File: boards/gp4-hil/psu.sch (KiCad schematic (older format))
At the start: 76 parts, among them K1 CONN_3_PWROUT, Q11 SSM6N58NU, Q12 DMP2069UFY4, U1 MIC2288-DFN, U20 SIP32408, U21 SIP32408, U22 SIP32408, U23 SIP32408, U24 SIP32408, U3 LTC3374-QFN, U4 SIP32408

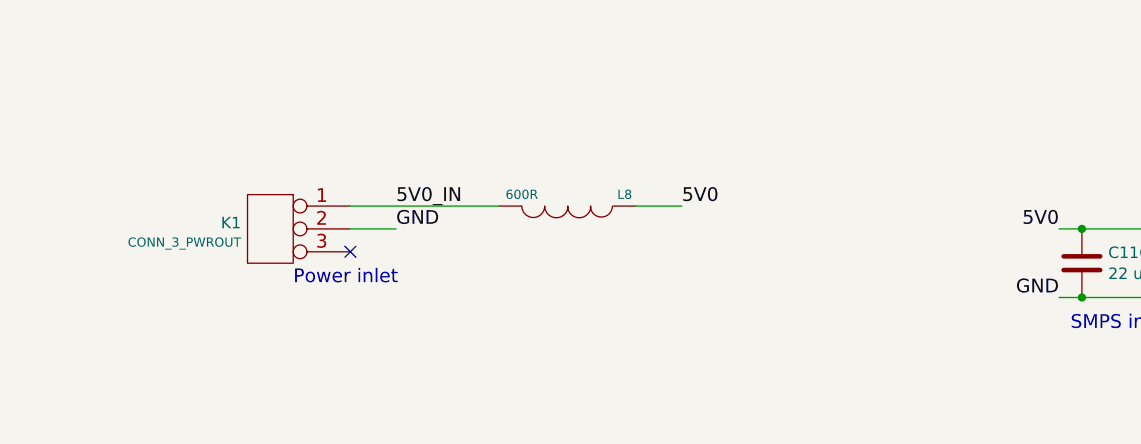
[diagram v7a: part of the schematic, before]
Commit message: Added reverse polarity protection and fusing to input
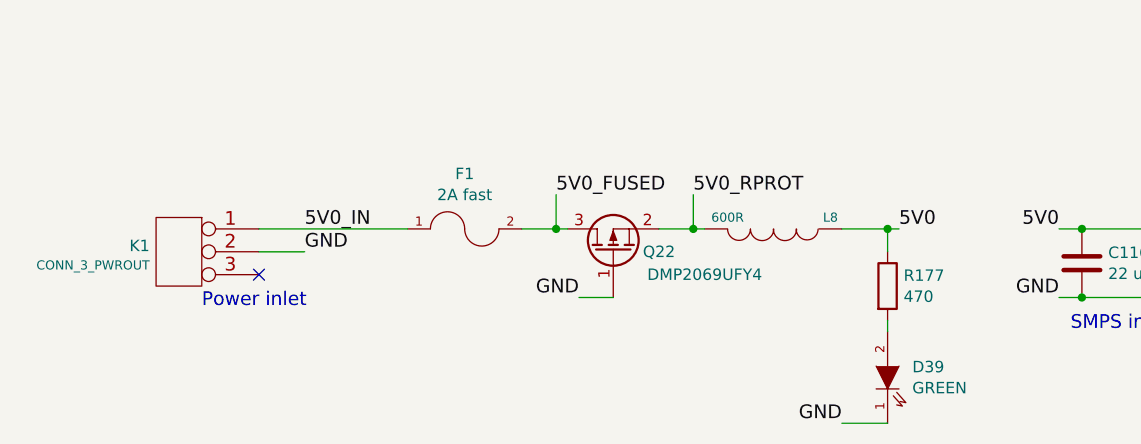
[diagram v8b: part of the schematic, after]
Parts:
- added D39: GREEN, symbol LED
- added F1: 2A fast, symbol FUSE
- added Q22: DMP2069UFY4, symbol Q_PMOS_GSD
- added R177: 470, symbol R
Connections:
- net 5V0: now also R177.1
- net 5V0_IN: now also F1.1; no longer L8.2
- net GND: now also D39.1 (K), Q22.1 (G)
- new net: D39.2 (A), R177.2
- new net 5V0_FUSED: F1.2, Q22.3 (D)
- new net 5V0_RPROT: L8.2, Q22.2 (S)
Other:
- moved on the sheet: K1, L8
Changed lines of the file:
@@
 	1    0    0    -1
 $EndComp
-Text Label 2250 15000 0    60   ~ 0
+Text Label 1850 15100 0    60   ~ 0
 5V0_IN
-Text Label 2250 15100 0    60   ~ 0
-GND
-NoConn ~ 2050 15200
-Text Notes 1800 15350 0    60   ~ 0
+Text Label 1850 15200 0    60   ~ 0
+GND
+NoConn ~ 1650 15300
+Text Notes 1400 15450 0    60   ~ 0
 Power inlet
 $Comp
 L CONN_3_PWROUT K1
 U 1 1 573DEBE1
-P 1700 15100
-F 0 "K1" H 1828 15126 50  0000 L CNN
-F 1 "CONN_3_PWROUT" H 1828 15041 40  0000 L CNN
-F 2 "" H 1700 15100 60  0000 C CNN
-F 3 "" H 1700 15100 60  0000 C CNN
-	1    1700 15100
+P 1300 15200
+F 0 "K1" H 1428 15226 50  0000 L CNN
+F 1 "CONN_3_PWROUT" H 1428 15141 40  0000 L CNN
+F 2 "" H 1300 15200 60  0000 C CNN
+F 3 "" H 1300 15200 60  0000 C CNN
+	1    1300 15200
 	-1   0    0    -1
 $EndComp
@@
 L INDUCTOR_PWROUT L8
 U 1 1 57402179
-P 3000 15000
-F 0 "L8" V 2950 15250 40  0000 C CNN
-F 1 "600R" V 2950 14800 40  0000 C CNN
-F 2 "" H 3000 15000 60  0000 C CNN
-F 3 "" H 3000 15000 60  0000 C CNN
-	1    3000 15000
-	0    1    1    0
-$EndComp
-Text Label 3500 15000 0    60   ~ 0
+P 3900 15100
+F 0 "L8" V 3850 15350 40  0000 C CNN
+F 1 "600R" V 3850 14900 40  0000 C CNN
+F 2 "" H 3900 15100 60  0000 C CNN
+F 3 "" H 3900 15100 60  0000 C CNN
+	1    3900 15100
+	0    1    1    0
+$EndComp
+Text Label 4450 15100 0    60   ~ 0
 5V0
 Text HLabel 4550 8550 2    60   Output ~ 0
@@
 Text Label 21050 3750 2    60   ~ 0
 PSU_VTEMP
-Wire Wire Line
-	2050 15000 2700 15000
-Wire Wire Line
-	2250 15100 2050 15100
+$Comp
+L FUSE F1
+U 1 1 5764BE84
+P 2550 15100
+F 0 "F1" H 2550 15341 50  0000 C CNN
+F 1 "2A fast" H 2550 15249 50  0000 C CNN
+F 2 "" H 2550 15100 60  0000 C CNN
+F 3 "" H 2550 15100 60  0000 C CNN
+	1    2550 15100
+	1    0    0    -1
+$EndComp
+$Comp
+L Q_PMOS_GSD Q22
+U 1 1 5764DB2D
+P 3200 15200
+F 0 "Q22" V 3200 15000 50  0000 C CNN
+F 1 "DMP2069UFY4" V 3100 14800 50  0000 C CNN
+F 2 "" H 3400 15300 29  0000 C CNN
+F 3 "" H 3200 15200 60  0000 C CNN
+	1    3200 15200
+	0    -1   -1   0
+$EndComp
+Text Label 2950 14950 0    60   ~ 0
+5V0_FUSED
+Text Label 3050 15400 2    60   ~ 0
+GND
+Text Label 3550 14950 0    60   ~ 0
+5V0_RPROT
+$Comp
+L LED D39
+U 1 1 576523BE
+P 4400 15750
+F 0 "D39" V 4446 15642 50  0000 R CNN
+F 1 "GREEN" V 4354 15642 50  0000 R CNN
+F 2 "" H 4400 15750 60  0000 C CNN
+F 3 "" H 4400 15750 60  0000 C CNN
+	1    4400 15750
+	0    -1   -1   0
+$EndComp
+$Comp
+L R R177
+U 1 1 57652BD8
+P 4400 15350
+F 0 "R177" H 4470 15396 50  0000 L CNN
+F 1 "470" H 4470 15304 50  0000 L CNN
+F 2 "" V 4330 15350 30  0000 C CNN
+F 3 "" H 4400 15350 30  0000 C CNN
+	1    4400 15350
+	1    0    0    -1
+$EndComp
+Wire Wire Line
+	1650 15100 2300 15100
+Wire Wire Line
+	1850 15200 1650 15200
 Wire Wire Line
 	900  1650 1900 1650
@@
 Connection ~ 3350 7800
 Wire Wire Line
-	3500 15000 3300 15000
+	4200 15100 4450 15100
 Wire Wire Line
 	3350 8250 3200 8250
@@
 Wire Wire Line
 	10750 4600 11150 4600
+Wire Wire Line
+	2800 15100 3000 15100
+Wire Wire Line
+	2950 14950 2950 15100
+Connection ~ 2950 15100
+Wire Wire Line
+	3050 15400 3200 15400
+Wire Wire Line
+	3600 15100 3400 15100
+Wire Wire Line
+	3550 14950 3550 15100
+Connection ~ 3550 15100
+Wire Wire Line
+	4400 15100 4400 15200
+Connection ~ 4400 15100
+Wire Wire Line
+	4400 15500 4400 15550
+Text Label 4200 15950 2    60   ~ 0
+GND
+Wire Wire Line
+	4200 15950 4400 15950
 $EndSCHEMATC
